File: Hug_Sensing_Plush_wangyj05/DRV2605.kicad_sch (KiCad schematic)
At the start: 10 parts, among them M1 EMR Motor, U4 DRV2605LDGS

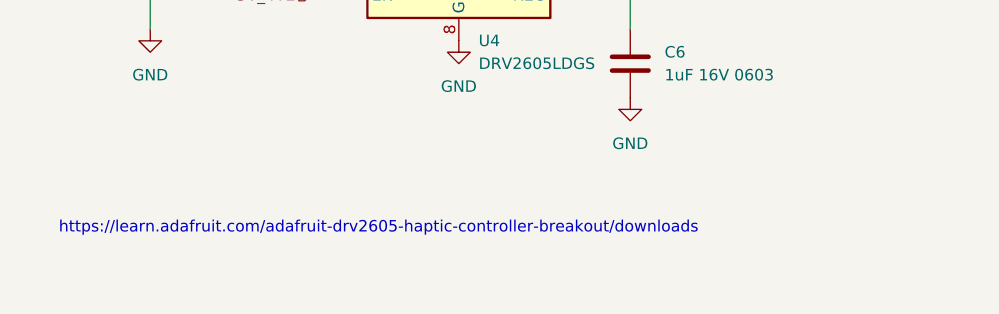
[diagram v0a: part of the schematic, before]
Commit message: Added more references
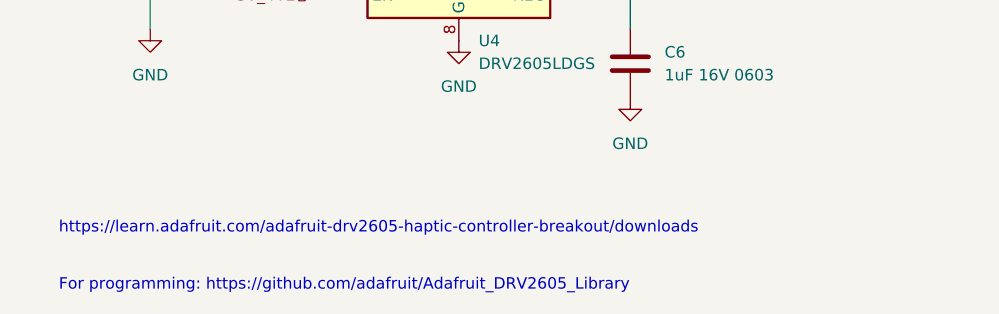
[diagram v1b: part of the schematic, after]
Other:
- note added: "For programming: https://github.com/adafruit/Adafruit_DRV2605_Library"
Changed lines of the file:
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@@
     (effects (font (size 1.27 1.27)) (justify left bottom))
+  )
+  (text "For programming: https://github.com/adafruit/Adafruit_DRV2605_Library"
+    (at 19.05 87.63 0)
+    (effects (font (size 1.27 1.27)) (justify left bottom) (href "https://github.com/adafruit/Adafruit_DRV2605_Library"))
   )
   (text "Powered by battery/battery charger" (at 62.23 21.59 0)
